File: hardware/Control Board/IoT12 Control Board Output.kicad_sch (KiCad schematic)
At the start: 24 parts, among them Q1 MMBT2222, Q2 MMBT2222, Q3 AOD403

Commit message: Start of next iteration.
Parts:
- removed A2: 2x Conn_01x09_Female, Display-extra:Nokia_5110_display_module, symbol Display_Graphic-extra:Nokia_5110_display
- removed J3, J4, J5: ~, TestPoint:TestPoint_THTPad_D2.0mm_Drill1.0mm, symbol Connector_Generic:Conn_01x01
- removed Q1: MMBT2222, Package_TO_SOT_SMD:SOT-23, symbol Transistor_BJT:BC817
- removed R32: 1k, Resistor_SMD:R_0805_2012Metric_Pad1.20x1.40mm_HandSolder, symbol Device:R
- removed R83: 1M, Resistor_SMD:R_0805_2012Metric_Pad1.20x1.40mm_HandSolder, symbol Device:R
- added J1: IDC-Header_2x07_P2.54mm, Connector_IDC:IDC-Header_2x07_P2.54mm_Vertical, symbol Connector_Generic:Conn_02x07_Odd_Even
- added J2: JST B2B-XH-A, Connector_JST:JST_XH_B2B-XH-A_1x02_P2.50mm_Vertical, symbol Connector:Conn_01x02_Male
- added J5: JST B5B-XH-A, Connector_JST:JST_XH_B5B-XH-A_1x05_P2.50mm_Vertical, symbol Connector:Conn_01x05_Male
- added R80: 560k, Resistor_SMD:R_0805_2012Metric_Pad1.20x1.40mm_HandSolder, symbol Device:R
- D10: renamed from D9; footprint Diode_SMD:D_SOT-23_ANK -> Package_TO_SOT_SMD:SOT-23
- NT2: renamed from NT4; footprint NetTie-extra:NetTie-2_SMD_Pad0.25mm -> NetTie-extra:NetTie-2_SMD_Pad0.5mm; now left out of the parts list
- NT3: renamed from NT5; footprint NetTie-extra:NetTie-2_SMD_Pad0.25mm -> NetTie-extra:NetTie-2_SMD_Pad0.5mm; now left out of the parts list
- R76: renamed from R82; value 1M -> 100k
- renumbered A3 to A2, D11 to D20, D5 to D30, D8 to D40, Q2 to Q1, Q3 to Q10, R34 to R32, R58 to R49, R59 to R50
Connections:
- net +24V: now also D10.3 (K); no longer D10.1 (K)
- net ESD: now also J5.3 (Pin_3)
- net GATE: now also D10.1 (A); no longer D10.2 (A)
- net GND: now also J1.3 (Pin_3), J1.5 (Pin_5), J1.7 (Pin_7), J1.9 (Pin_9)
- net I2S_SD: now also R80.2; no longer A2.5 (SD)
- net IRON_+: now also J5.5 (Pin_5)
- net IRON_-: now also J5.4 (Pin_4)
- net at A2.8 (SPK-): now also J2.2 (Pin_2)
- net at A2.9 (SPK+): now also J2.1 (Pin_1)
- new net: A2.5 (SD), R80.1
- new net +3.3V: J1.1 (Pin_1)
- new net NTC_IN: J5.2 (Pin_2)
- new net SHAKE_IN: J5.1 (Pin_1)
- new net TFT_D~{C}: J1.2 (Pin_2)
- new net TFT_LED: J1.11 (Pin_11)
- new net TFT_MISO: J1.8 (Pin_8)
- new net TFT_MOSI: J1.6 (Pin_6)
- new net TFT_SCLK: J1.4 (Pin_4)
- new net TFT_~{CS}: J1.10 (Pin_10)
- new net TFT_~{RST}: J1.12 (Pin_12)
- new net TOUCH_~{CS}: J1.13 (Pin_13)
- new net TOUCH_~{IRQ}: J1.14 (Pin_14)
- no-connect marks 2 -> 0
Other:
- note added: "Display 2.8" 320x240 TFT Touch SKU: MSP2807 Display: ILI9341 Touch: XPT2046"
- note added: "Mono I2S audio amplifier"
- note removed: "Bleep bloop module"
- note removed: "Display"
- company: (none) -> https://github.com/atoomnetmarc/IoT12
- title: IoT12-hardware output -> IoT12 Control Board
- moved on the sheet: A2, D20, NT2, NT3, R1, R50, R71, R72, R76

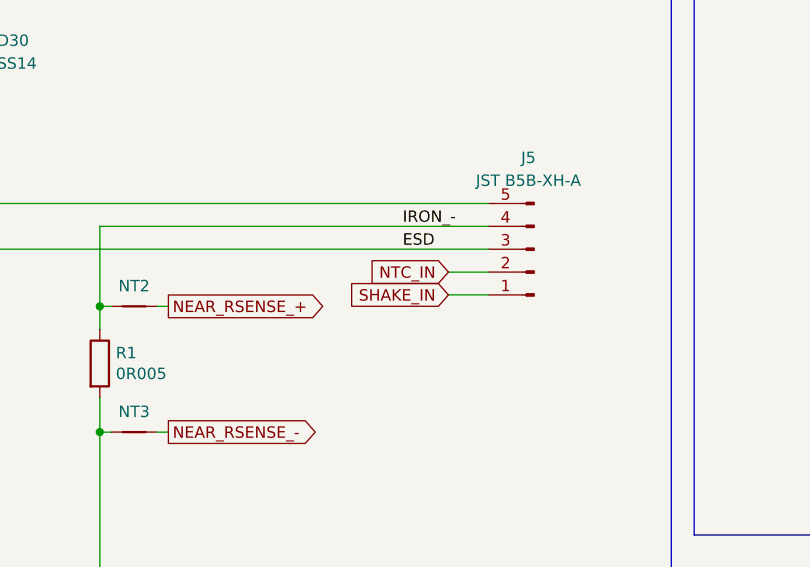
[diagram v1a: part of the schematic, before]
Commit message: Update Control Board project to Kicad 7.0.2
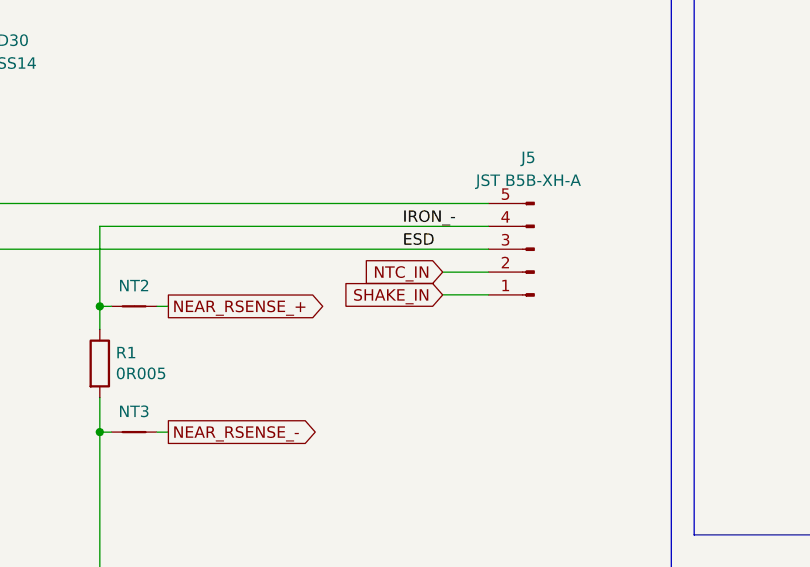
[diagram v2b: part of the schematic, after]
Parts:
- J2: symbol Connector:Conn_01x02_Male -> Connector:Conn_01x02_Pin
- J5: symbol Connector:Conn_01x05_Male -> Connector:Conn_01x05_Pin
